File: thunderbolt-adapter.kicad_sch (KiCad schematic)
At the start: 29 parts

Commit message: Connect power supplies (WiP)
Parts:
- added C? (x2): C_10u_0402, antmicro-footprints:0402-cap, symbol antmicroCapacitors0402:C_10u_0402
- added C? (x7): C_1u_0402, antmicro-footprints:0402-cap, symbol antmicroCapacitors0402:C_1u_0402
- added C? (x4): C_22u_0603, antmicro-footprints:0603-cap, symbol antmicroCapacitors0603:C_22u_0603
- added L?: IHLP1616BZERR68M5A, antmicro-footprints:IHLP1616BZ, symbol antmicroFixedInductors:IHLP1616BZERR68M5A
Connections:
- net GND: now also C?.2, C?.2, C?.2, C?.2, C?.2, C?.2, C?.2, C?.2, C?.2, C?.2, C?.2, C?.2, C?.2
- net at U?.C1 (SVR_IND): now also U?.C2 (SVR_IND), U?.D1 (SVR_IND), L?.1 (P)
- net at U?.E12 (VCC0P9_SVR_ANA): now also U?.E13 (VCC0P9_SVR_ANA), U?.F11 (VCC0P9_SVR_ANA), U?.F12 (VCC0P9_SVR_ANA), U?.F13 (VCC0P9_SVR_ANA), U?.F15 (VCC0P9_SVR_ANA), U?.J9 (VCC0P9_SVR_SENSE), U?.L9 (VCC0P9_SVR), U?.M9 (VCC0P9_SVR), C?.1, C?.1, C?.1, C?.1, C?.1, C?.1, C?.1, C?.1, C?.1, L?.2 (P)
- net at U?.F18 (VCC0P9_LVR): now also U?.H11 (VCC0P9_LVR_SENSE), U?.H18 (VCC0P9_LVR), U?.J11 (VCC0P9_LVR), C?.1, C?.1, C?.1, C?.1
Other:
- moved on the sheet: U?A

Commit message: Prepare PCB mock
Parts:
- added C25, C26: C_10p_0402, antmicro-footprints:0402-cap, symbol antmicroCapacitors0402:C_10p_0402
- added N1: antmicro_logo, antmicro-footprints:antmicro-logo, symbol antmicroMechanicalParts:antmicro_logo
- added U3: TPS65983BAZBHR, antmicro-footprints:TPS65983BAZBHR, symbol antmicroInterfaceControllers:TPS65983BAZBHR
- added U5: MX25L8006EM1I-12G, antmicro-footprints:SOIC-8_W3.9mm, symbol antmicroMemory:MX25L8006EM1I-12G
- added Y2: 25MHz, antmicro-footprints:KX-7, symbol antmicroCrystals:ABM8G-25.000MHZ-B4Y-T
- U4: renamed from U?; footprint (none) -> antmicro-footprints:JHL6340SLLSQ
- gave numbers to parts that had none: 42
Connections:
- net GND: now also C25.1, C26.1, U3.A1 (GND), U3.B8 (GND), U3.D8 (GND), U3.E5 (GND), U3.E6 (GND), U3.E7 (GND), U3.E8 (GND), U3.F5 (GND), U3.F6 (GND), U3.F7 (GND), U3.F8 (GND), U3.G5 (GND), U3.G6 (GND), U3.G7 (GND), U3.G8 (GND), U3.H4 (GND), U3.H5 (GND), U3.H8 (GND), U3.L1 (GND), Y2.2
- new net: C26.2, Y2.1
- new net: C25.2, Y2.3
- new net PP_5V0: U3.A11 (PP_5V0), U3.B11 (PP_5V0), U3.C11 (PP_5V0), U3.D11 (PP_5V0)
- new net PP_HV: U3.A6 (PP_HV), U3.A7 (PP_HV), U3.A8 (PP_HV), U3.B7 (PP_HV)
- new net VBUS: U3.H11 (VBUS), U3.J10 (VBUS), U3.J11 (VBUS), U3.K11 (VBUS)

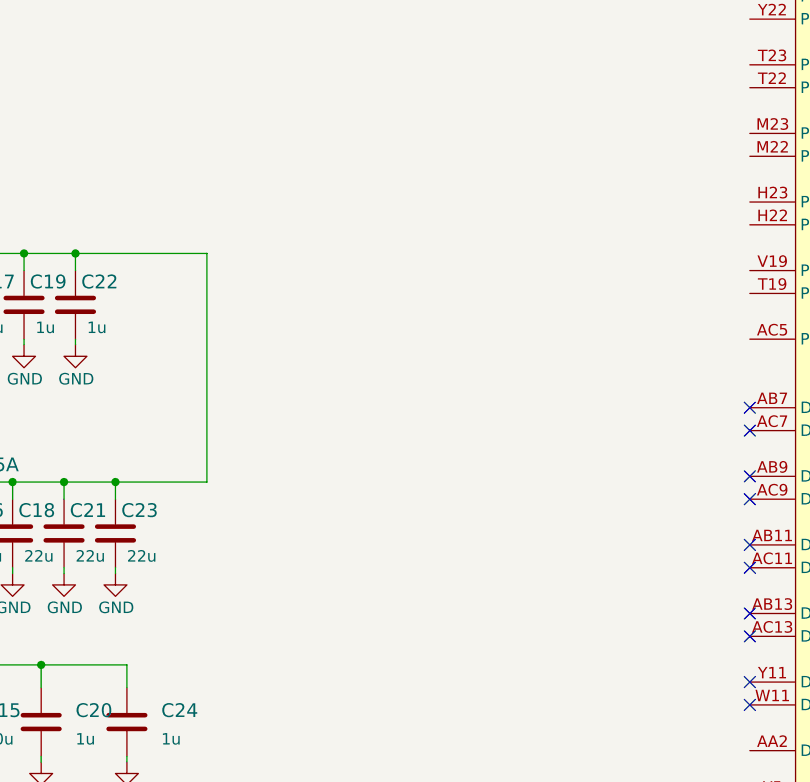
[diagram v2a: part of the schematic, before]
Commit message: Add 0.9V LED indicator
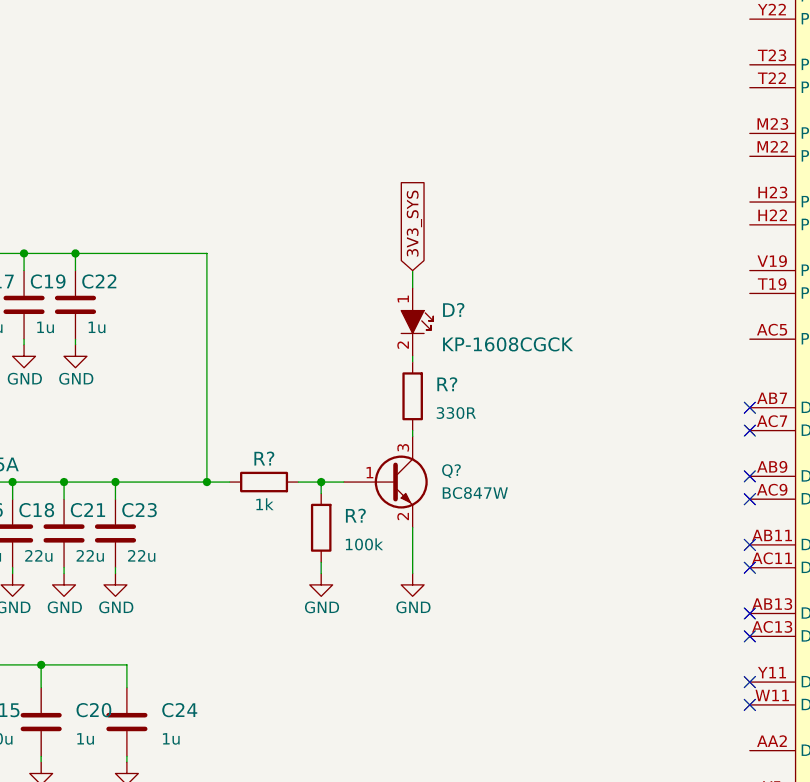
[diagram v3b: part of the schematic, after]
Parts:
- added D?: KP-1608CGCK, antmicro-footprints:LED_0603, symbol antmicroLEDIndicationDiscrete:KP-1608CGCK
- added Q?: BC847W, antmicro-footprints:SOT-323, symbol antmicroTransistorsBipolarSingle:BC847W
- added R?: R_1k_0402, antmicro-footprints:0402-res, symbol antmicroResistors0402:R_1k_0402
- added R?: R_100k_0402, antmicro-footprints:0402-res, symbol antmicroResistors0402:R_100k_0402
- added R?: R_330R_0402, antmicro-footprints:0402-res, symbol antmicroResistors0402:R_330R_0402
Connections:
- net 3V3_SYS: now also D?.1
- net GND: now also Q?.2 (E), R?.1
- net at C12.1, C14.1, C16.1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: now also R?.1
- new net: Q?.1 (B), R?.2, R?.2
- new net: D?.2, R?.2
- new net: Q?.3 (C), R?.1

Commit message: Connect USB-C controller (WiP)
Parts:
- removed C25, C26: C_10p_0402, antmicro-footprints:0402-cap, symbol antmicroCapacitors0402:C_10p_0402
- removed N1: antmicro_logo, antmicro-footprints:antmicro-logo, symbol antmicroMechanicalParts:antmicro_logo
- removed Y2: 25MHz, antmicro-footprints:KX-7, symbol antmicroCrystals:ABM8G-25.000MHZ-B4Y-T
- added C? (x19): C_1u_0402, antmicro-footprints:0402-cap, symbol antmicroCapacitors0402:C_1u_0402
- added C?: C_4u7_0402_25V, antmicro-footprints:0402-cap, symbol antmicroCapacitors0402:C_4u7_0402_25V
- added C? (x2): C_10p_0402, antmicro-footprints:0402-cap, symbol antmicroCapacitors0402:C_10p_0402
- added C?: C_220n_0402, antmicro-footprints:0402-cap, symbol antmicroCapacitors0402:C_220n_0402
- added C?: C_100n_0402, antmicro-footprints:0402-cap, symbol antmicroCapacitors0402:C_100n_0402
- added R?: R_15k_0.1%_0402, antmicro-footprints:0402-res, symbol antmicroResistors0402:R_15k_0.1%_0402
- added R?: R_4k75_0.5%_0402, antmicro-footprints:0402-res, symbol antmicroResistors0402:R_4k75_0.5%_0402
- added R? (x2): R_100R_0402, antmicro-footprints:0402-res, symbol antmicroResistors0402:R_100R_0402
- added TP?: TP_SMD1MM, antmicro-footprints:Testpoint_smd_1mm, symbol antmicroTestPoints:TP_SMD1MM
- added Y?: 25MHz, antmicro-footprints:KX-7, symbol antmicroCrystals:ABM8G-25.000MHZ-B4Y-T
- U4: footprint (none) -> antmicro-footprints:JHL6340SLLSQ
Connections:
- net 3V3_SYS: now also U5.8 (VCC), C?.1
- net GND: now also U5.4 (GND), C?.1, C?.1, C?.2, C?.2, C?.2, C?.2, C?.2, C?.2, C?.2, C?.2, C?.2, C?.2, C?.2, C?.2, C?.2, C?.2, C?.2, C?.2, C?.2, C?.2, C?.2, C?.2, C?.2, C?.2, R?.2, R?.2, R?.2, Y?.2, Y?.4
- net PP_HV: now also C?.1
- net at C12.1, C14.1, C16.1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: now also TP?.1
- net at U3.G2 (R_OSC): now also R?.1
- net at U3.H7 (SS): now also C?.1
- net at U4.AB5 (TEST_PWR_GOOD): now also R?.1
- net at U4.D22 (XTAL_25_IN): now also C?.2, Y?.1
- net at U4.D23 (XTAL_25_OUT): now also C?.2, Y?.3
- net at U4.E1 (TEST_EN): now also R?.1
- net at U4.H6 (RBIAS): now also R?.2
- net at U4.J6 (RSENSE): now also R?.1
- net at U4.J16 (VCC3P3_ANA_USB2): now also C?.1
- net at U4.L11 (VCC0P9_DP): now also U4.L12 (VCC0P9_DP), U4.L6 (VCC0P9_ANA_DPSRC), U4.L8 (VCC0P9_DP), U4.M6 (VCC0P9_ANA_DPSRC), U4.M8 (VCC0P9_DP), U4.T11 (VCC0P9_DP), U4.T12 (VCC0P9_DP), U4.V11 (VCC0P9_ANA_DPSNK), U4.V12 (VCC0P9_ANA_DPSNK), U4.V13 (VCC0P9_ANA_DPSNK), C?.1, C?.1, C?.1, C?.1, C?.1, C?.1
- net at U4.L16 (VCC3P3_ANA_PCIE): now also C?.1
- net at U4.L18 (VCC0P9_ANA_PCIE_2): now also U4.L19 (VCC0P9_ANA_PCIE_1), U4.M13 (VCC0P9_PCIE), U4.M15 (VCC0P9_PCIE), U4.M16 (VCC0P9_PCIE), U4.M18 (VCC0P9_ANA_PCIE_2), U4.N18 (VCC0P9_ANA_PCIE_2), U4.N19 (VCC0P9_ANA_PCIE_1), C?.1, C?.1, C?.1, C?.1, C?.1
- net at U4.R11 (VCC0P9_CIO): now also U4.R12 (VCC0P9_CIO), U4.R8 (VCC0P9_CIO), U4.R9 (VCC0P9_CIO), C?.1, C?.1, C?.1, C?.1
- net at U4.R15 (VCC0P9_USB): now also U4.R16 (VCC0P9_USB), C?.1, C?.1
- no-connect marks 62 -> 73
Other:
- moved on the sheet: C1, C10, C11, C12, C13, C14, C15, C16, C17, C18, C19, C2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

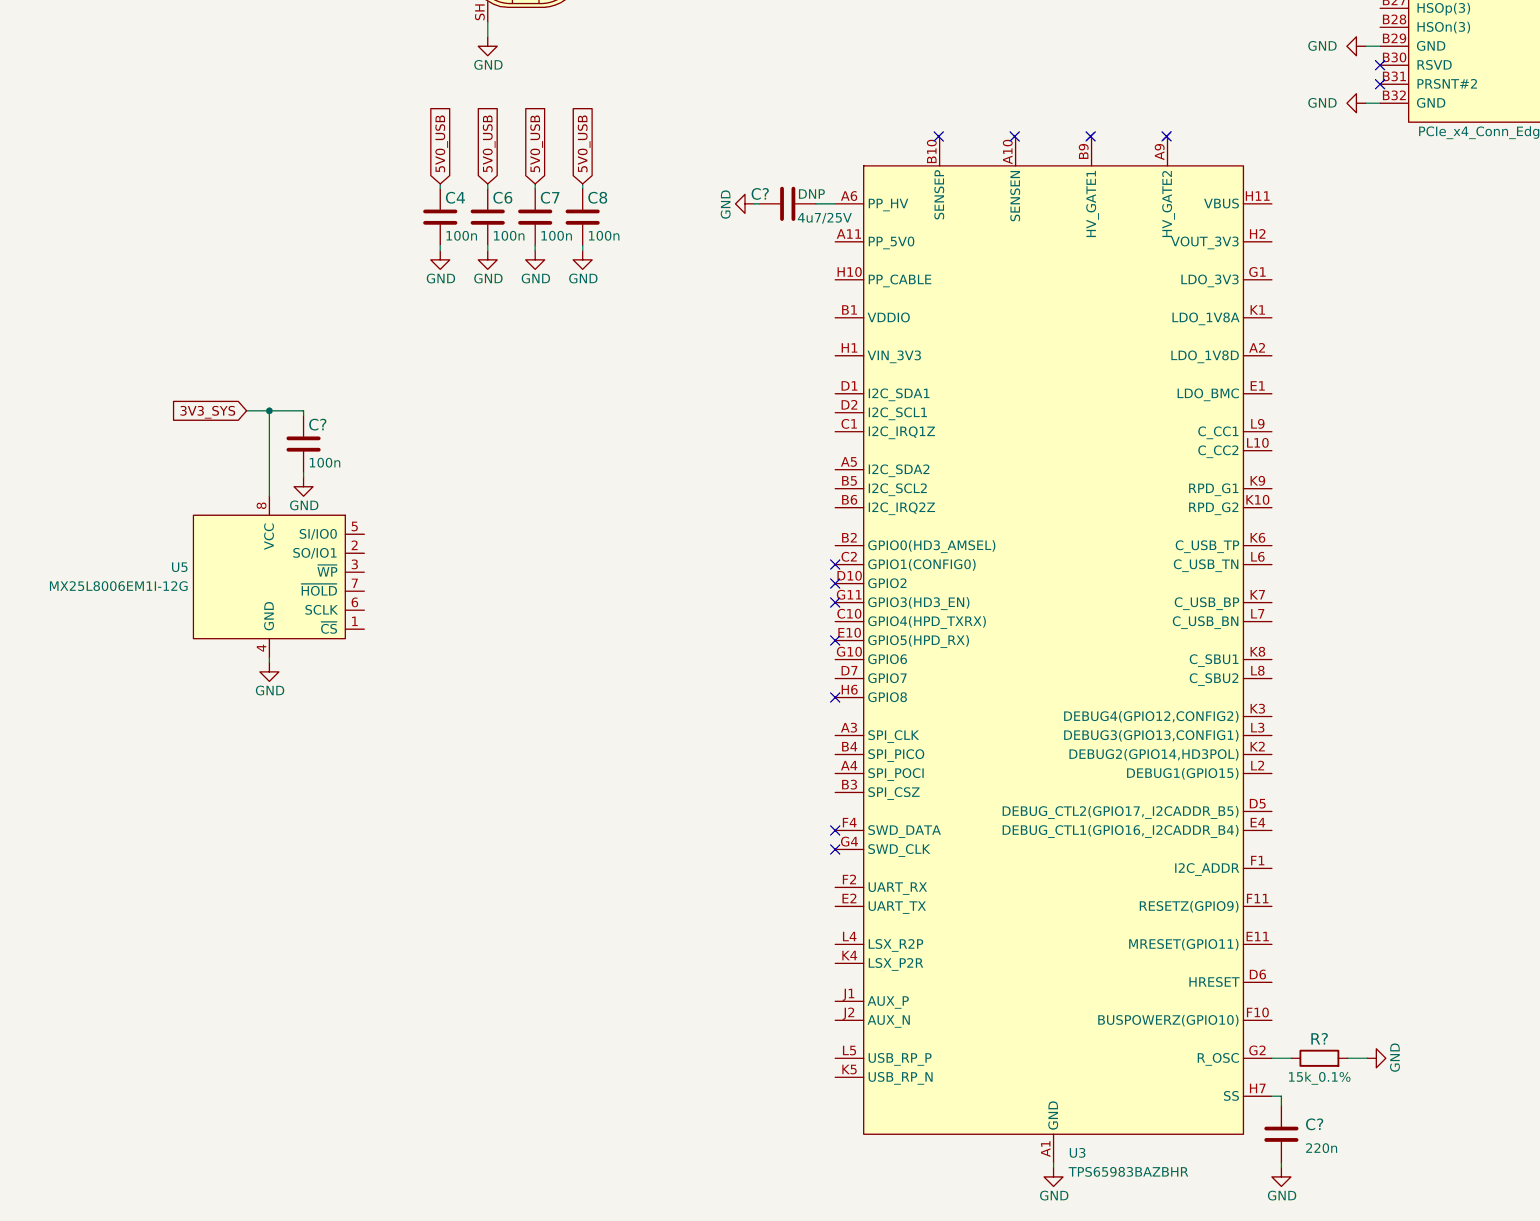
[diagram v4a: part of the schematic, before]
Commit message: Unify grid on the sch
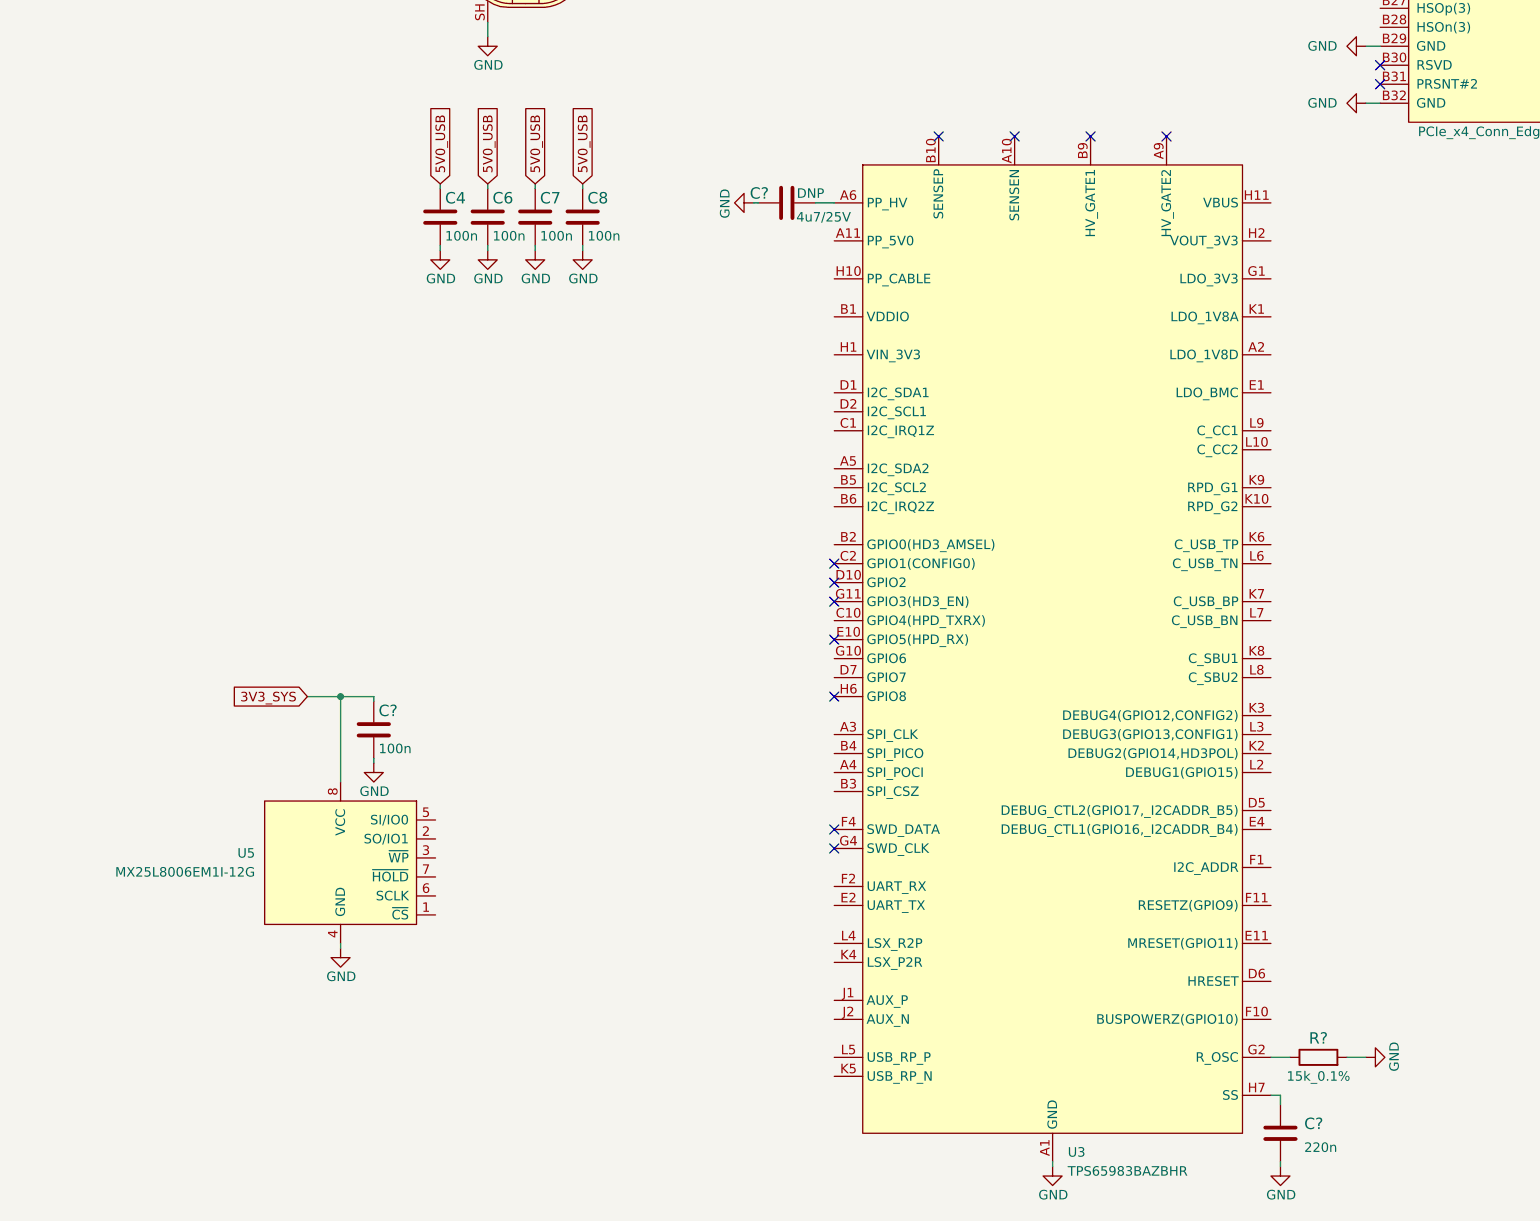
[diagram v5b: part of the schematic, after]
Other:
- moved on the sheet: C?

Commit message: Continue connecting TPS65983 power and signals
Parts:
- added C? (x2): C_100n_0402, antmicro-footprints:0402-cap, symbol antmicroCapacitors0402:C_100n_0402
- added C? (x2): C_10u_0402, antmicro-footprints:0402-cap, symbol antmicroCapacitors0402:C_10u_0402
- added C? (x2): C_1u_0402, antmicro-footprints:0402-cap, symbol antmicroCapacitors0402:C_1u_0402
- added C?: C_4u7_0402, antmicro-footprints:0402-cap, symbol antmicroCapacitors0402:C_4u7_0402
- added C? (x2): C_22u_0805_25V, antmicro-footprints:0805-cap, symbol antmicroCapacitorsmisc:C_22u_0805_25V
- added R? (x2): R_100k_0402, antmicro-footprints:0402-res, symbol antmicroResistors0402:R_100k_0402
- added R?: R_0R_0603, antmicro-footprints:0603-res, symbol antmicroResistors0603:R_0R_0603
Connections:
- net 3V3_SYS: now also U3.B1 (VDDIO), U3.H1 (VIN_3V3), C?.1, C?.1
- net 5V0_USB: now also R?.2
- net GND: now also C?.1, C?.2, C?.2, C?.2, C?.2, C?.2, C?.2, R?.2
- net PP_5V0: now also U3.H10 (PP_CABLE), C?.2
- net VBUS: now also C?.1, C?.1, R?.1
- net TPS_3V3: now reaches U3.G1 (LDO_3V3)
- net TPS_3V3: now also C?.1, R?.2
- net at U3.H2 (VOUT_3V3): now also C?.1
- net AUX_P: now reaches U3.J1 (AUX_P)
- net AUX_P: now also C?.1, R?.1
- net AUX_N: now reaches U3.J2 (AUX_N)
- net AUX_N: now also C?.1, R?.1
- net at U4.W15 (PA_DPSRC_AUX_N): now also C?.2
- net at U4.Y15 (PA_DPSRC_AUX_P): now also C?.2
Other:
- moved on the sheet: J2

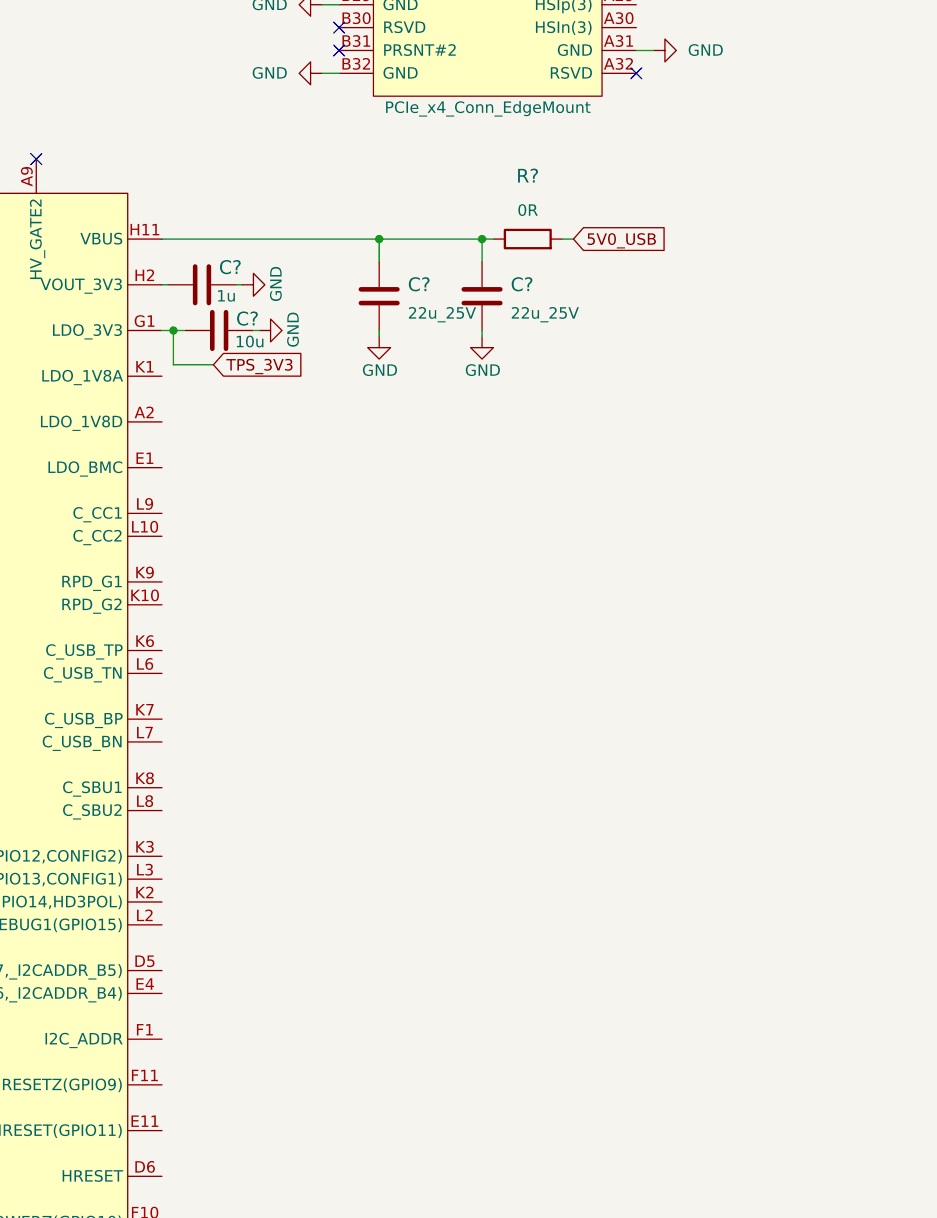
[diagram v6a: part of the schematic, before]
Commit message: Connect TPS65983 power pins
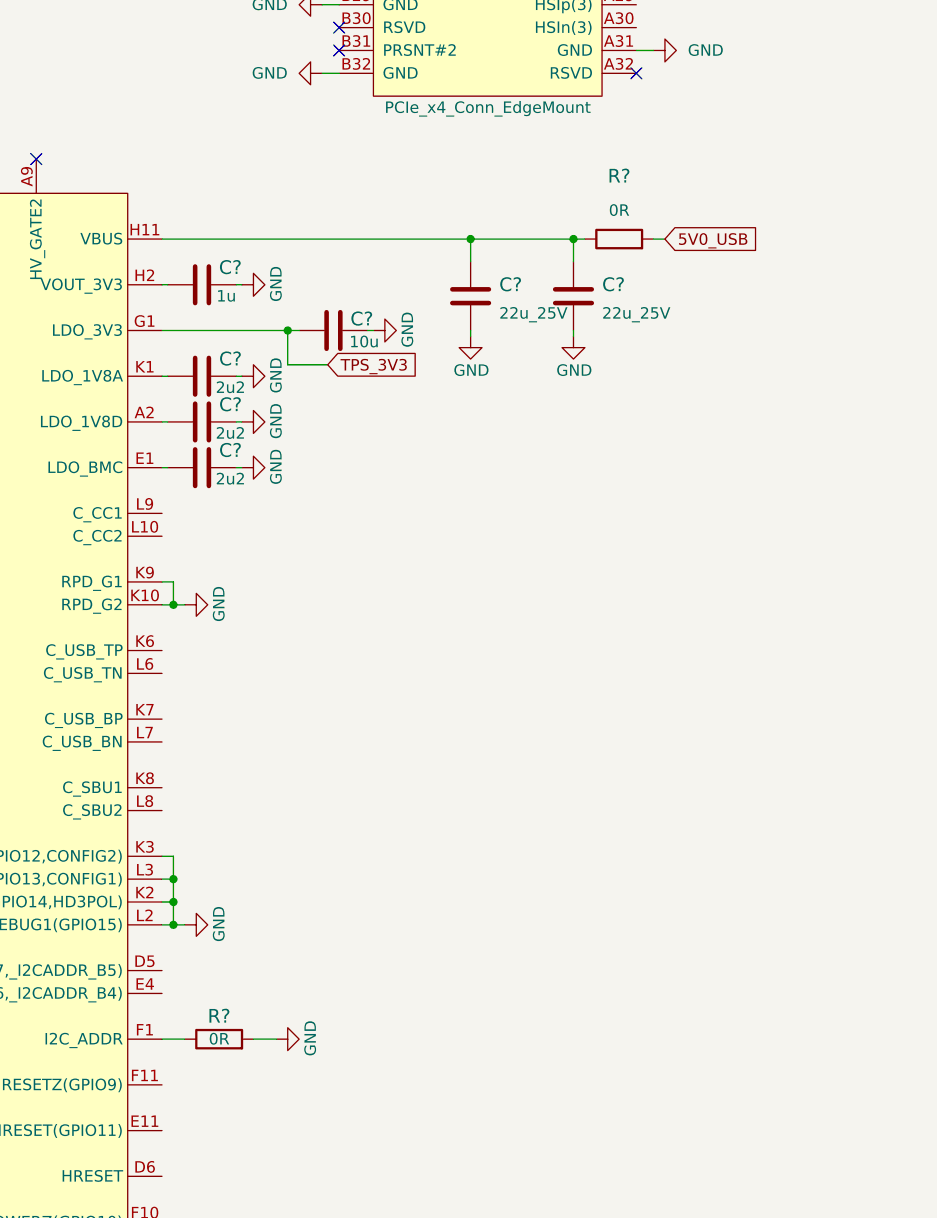
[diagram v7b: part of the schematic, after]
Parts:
- added C? (x3): C_2u2_0402, antmicro-footprints:0402-cap, symbol antmicroCapacitors0402:C_2u2_0402
- added R?: R_0R_0402, antmicro-footprints:0402-res, symbol antmicroResistors0402:R_0R_0402
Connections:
- net GND: now also U3.K10 (RPD_G2), U3.K2 (DEBUG2(GPIO14,HD3POL)), U3.K3 (DEBUG4(GPIO12,CONFIG2)), U3.K9 (RPD_G1), U3.L2 (DEBUG1(GPIO15)), U3.L3 (DEBUG3(GPIO13,CONFIG1)), C?.2, C?.2, C?.2, R?.2
- net at U3.A2 (LDO_1V8D): now also C?.1
- net at U3.E1 (LDO_BMC): now also C?.1
- net at U3.F1 (I2C_ADDR): now also R?.1
- net at U3.K1 (LDO_1V8A): now also C?.1
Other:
- moved on the sheet: C?, R?
